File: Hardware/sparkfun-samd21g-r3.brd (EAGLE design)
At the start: 57.1 x 53.3 mm, 62 parts, among them Q1 2.5A/30V, Q2 2N7002PW, U1 MCP73831, U2 74AHC1G125, U3 MIC5219 3.3V, U4 ATSAMD21G-A, Y1 32.768kHz

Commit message: Swapping MIC5205 Regulator out for AP2112K-3.3V
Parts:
- U3: value MIC5219 3.3V -> 3.3V
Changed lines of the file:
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@@
 <layer number="47" name="Measures" color="7" fill="1" visible="no" active="yes"/>
 <layer number="48" name="Document" color="7" fill="1" visible="no" active="yes"/>
-<layer number="49" name="Reference" color="7" fill="1" visible="yes" active="yes"/>
+<layer number="49" name="Reference" color="7" fill="1" visible="no" active="yes"/>
 <layer number="50" name="dxf" color="7" fill="1" visible="no" active="no"/>
 <layer number="51" name="tDocu" color="6" fill="1" visible="yes" active="yes"/>
@@
 <attribute name="PROD_ID" value="IC-13064" x="38.1" y="30.48" size="1.778" layer="27" rot="R180" display="off"/>
 </element>
-<element name="U3" library="SparkFun-PowerIC" package="SOT23-5" value="MIC5219 3.3V" x="17.78" y="10.16" rot="R270">
-<attribute name="PROD_ID" value="VREG-09872" x="17.78" y="10.16" size="1.778" layer="27" rot="R270" display="off"/>
+<element name="U3" library="SparkFun-PowerIC" package="SOT23-5" value="3.3V" x="17.78" y="10.16" rot="R270">
+<attribute name="PROD_ID" value="VREG-12457" x="17.78" y="10.16" size="1.778" layer="27" rot="R270" display="off"/>
 </element>
 <element name="JP2" library="SparkFun-Connectors" package="USB-AB-MICRO-SMD_V03" value="" x="2.286" y="40.64">

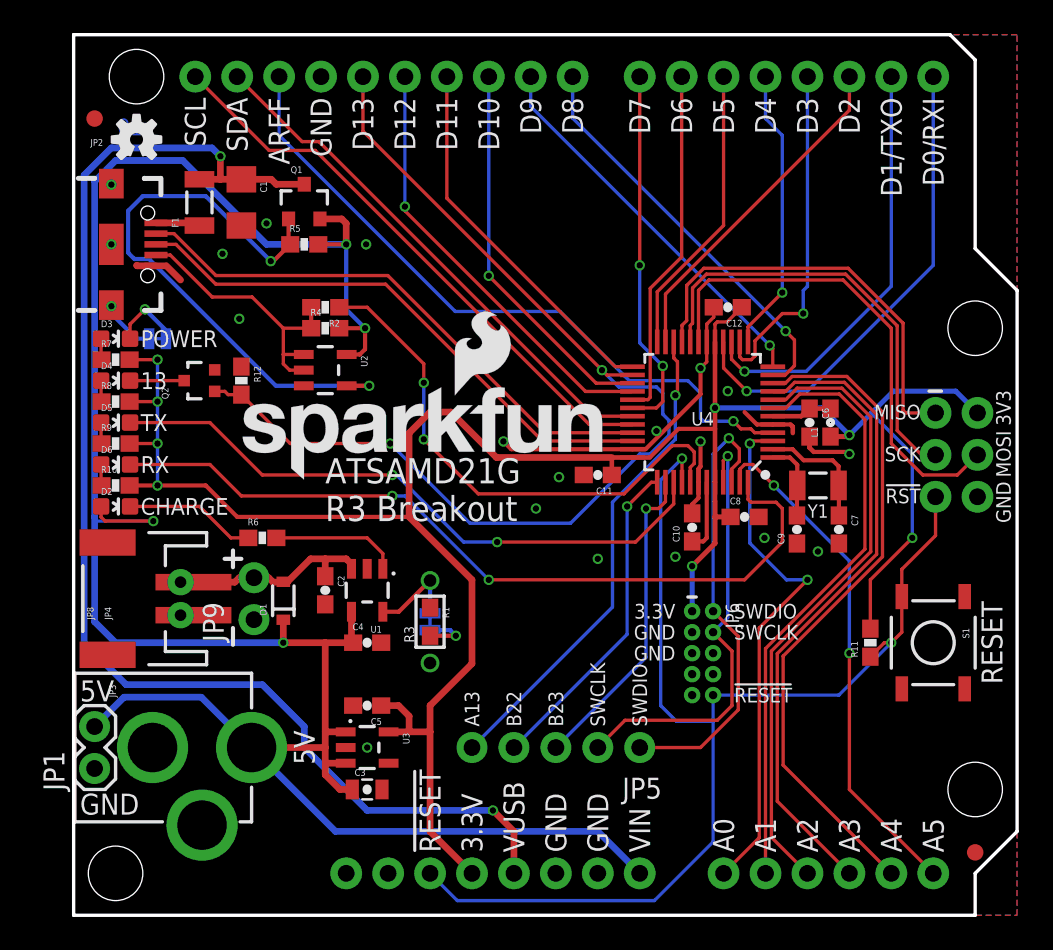
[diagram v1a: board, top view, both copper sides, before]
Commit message: Adding pin numbers to middle-board pins. Adding PWM indicators.
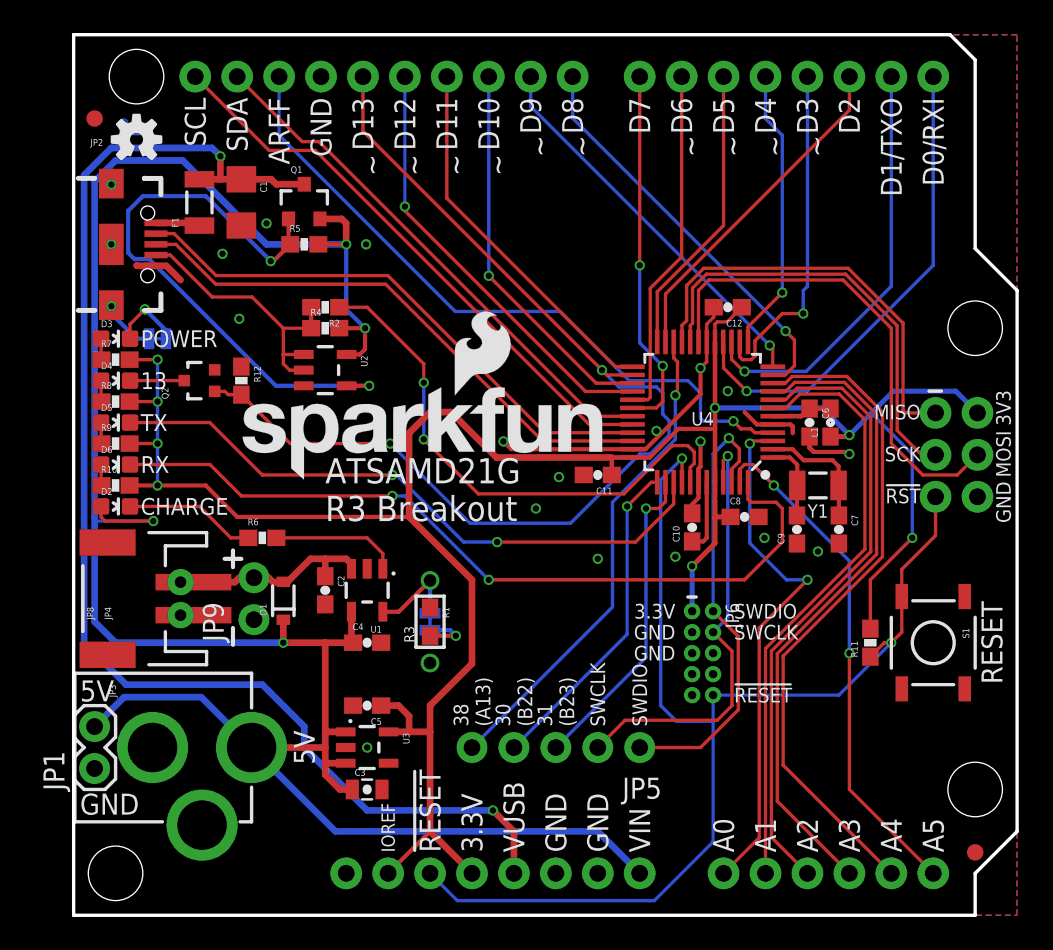
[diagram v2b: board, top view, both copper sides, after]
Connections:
- net 3.3V: now also JP7.IOREF
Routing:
- net 3.3V: track 143.7 -> 147.2 mm
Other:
- board text added: "30 (B22)"
- board text added: "31 (B23)"
- board text added: "38 (A13)"
- board text added: "IOREF"
- board text added: "~"
- board text removed: "A13"
- board text removed: "B22"
- board text removed: "B23"
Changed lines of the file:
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@@
 <layer number="47" name="Measures" color="7" fill="1" visible="no" active="yes"/>
 <layer number="48" name="Document" color="7" fill="1" visible="no" active="yes"/>
-<layer number="49" name="Reference" color="7" fill="1" visible="no" active="yes"/>
+<layer number="49" name="Reference" color="7" fill="1" visible="yes" active="yes"/>
 <layer number="50" name="dxf" color="7" fill="1" visible="no" active="no"/>
 <layer number="51" name="tDocu" color="6" fill="1" visible="yes" active="yes"/>
@@
 <text x="40.005" y="18.415" size="0.889" layer="21" font="vector" ratio="15" align="center-left">SWDIO</text>
 <text x="40.005" y="17.145" size="0.889" layer="21" font="vector" ratio="15" align="center-left">SWCLK</text>
-<text x="24.13" y="11.43" size="0.889" layer="21" font="vector" ratio="15" rot="R90" align="center-left">A13</text>
-<text x="26.67" y="11.43" size="0.889" layer="21" font="vector" ratio="15" rot="R90" align="center-left">B22</text>
-<text x="29.21" y="11.43" size="0.889" layer="21" font="vector" ratio="15" rot="R90" align="center-left">B23</text>
+<text x="24.13" y="11.43" size="0.889" layer="21" font="vector" ratio="15" rot="R90" align="center-left">38
+(A13)</text>
+<text x="26.67" y="11.43" size="0.889" layer="21" font="vector" ratio="15" rot="R90" align="center-left">30
+(B22)</text>
+<text x="29.21" y="11.43" size="0.889" layer="21" font="vector" ratio="15" rot="R90" align="center-left">31
+(B23)</text>
 <text x="20.32" y="17.78" size="0.889" layer="22" font="vector" ratio="15" rot="MR270" align="bottom-center">R-Prog</text>
 <text x="21.59" y="3.81" size="1.27" layer="22" font="vector" ratio="15" rot="MR270" align="center-right">!RESET!</text>
@@
 <wire x1="10.922" y1="16.637" x2="10.922" y2="15.621" width="0.254" layer="22"/>
 <wire x1="51.816" y1="31.75" x2="52.578" y2="31.75" width="0.2032" layer="21"/>
-<text x="24.13" y="11.43" size="0.889" layer="22" font="vector" ratio="15" rot="MR90" align="center-left">A13</text>
-<text x="26.67" y="11.43" size="0.889" layer="22" font="vector" ratio="15" rot="MR90" align="center-left">B22</text>
-<text x="29.21" y="11.43" size="0.889" layer="22" font="vector" ratio="15" rot="MR90" align="center-left">B23</text>
 <text x="31.75" y="11.43" size="0.889" layer="22" font="vector" ratio="15" rot="MR90" align="center-left">SWCLK</text>
 <text x="34.29" y="11.43" size="0.889" layer="22" font="vector" ratio="15" rot="MR90" align="center-left">SWDIO</text>
+<text x="24.13" y="11.43" size="0.889" layer="22" font="vector" ratio="15" rot="MR90" align="center-left">38
+(A13)</text>
+<text x="26.67" y="11.43" size="0.889" layer="22" font="vector" ratio="15" rot="MR90" align="center-left">30
+(B22)</text>
+<text x="29.21" y="11.43" size="0.889" layer="22" font="vector" ratio="15" rot="MR90" align="center-left">31
+(B23)</text>
+<text x="19.05" y="3.81" size="0.8128" layer="21" font="vector" ratio="15" rot="R90" align="center-left">IOREF</text>
+<text x="19.05" y="3.81" size="1.27" layer="22" font="vector" ratio="15" rot="MR90" align="center-left">IOREF</text>
+<text x="44.958" y="47.244" size="1.27" layer="21" font="vector" ratio="15" rot="R90" align="center-right">~</text>
+<text x="42.418" y="47.244" size="1.27" layer="21" font="vector" ratio="15" rot="R90" align="center-right">~</text>
+<text x="39.878" y="47.244" size="1.27" layer="21" font="vector" ratio="15" rot="R90" align="center-right">~</text>
+<text x="37.338" y="47.244" size="1.27" layer="21" font="vector" ratio="15" rot="R90" align="center-right">~</text>
+<text x="30.734" y="47.244" size="1.27" layer="21" font="vector" ratio="15" rot="R90" align="center-right">~</text>
+<text x="28.194" y="47.244" size="1.27" layer="21" font="vector" ratio="15" rot="R90" align="center-right">~</text>
+<text x="25.654" y="46.101" size="1.27" layer="21" font="vector" ratio="15" rot="R90" align="center-right">~</text>
+<text x="23.114" y="46.101" size="1.27" layer="21" font="vector" ratio="15" rot="R90" align="center-right">~</text>
+<text x="20.574" y="46.101" size="1.27" layer="21" font="vector" ratio="15" rot="R90" align="center-right">~</text>
+<text x="18.034" y="46.101" size="1.27" layer="21" font="vector" ratio="15" rot="R90" align="center-right">~</text>
+<text x="17.018" y="46.101" size="1.27" layer="22" font="vector" ratio="15" rot="MR90" align="center-right">~</text>
+<text x="19.558" y="46.101" size="1.27" layer="22" font="vector" ratio="15" rot="MR90" align="center-right">~</text>
+<text x="22.098" y="46.101" size="1.27" layer="22" font="vector" ratio="15" rot="MR90" align="center-right">~</text>
+<text x="24.638" y="46.101" size="1.27" layer="22" font="vector" ratio="15" rot="MR90" align="center-right">~</text>
+<text x="27.178" y="47.244" size="1.27" layer="22" font="vector" ratio="15" rot="MR90" align="center-right">~</text>
+<text x="29.718" y="47.244" size="1.27" layer="22" font="vector" ratio="15" rot="MR90" align="center-right">~</text>
+<text x="36.322" y="47.244" size="1.27" layer="22" font="vector" ratio="15" rot="MR90" align="center-right">~</text>
+<text x="38.862" y="47.244" size="1.27" layer="22" font="vector" ratio="15" rot="MR90" align="center-right">~</text>
+<text x="41.402" y="47.244" size="1.27" layer="22" font="vector" ratio="15" rot="MR90" align="center-right">~</text>
+<text x="43.942" y="47.244" size="1.27" layer="22" font="vector" ratio="15" rot="MR90" align="center-right">~</text>
 </plain>
 <attributes>
@@
 <wire x1="8.001" y1="26.035" x2="5.08" y2="26.035" width="0.254" layer="1"/>
 <wire x1="3.39" y1="26.035" x2="5.08" y2="26.035" width="0.254" layer="1"/>
+<contactref element="JP7" pad="IOREF"/>
+<wire x1="19.05" y1="2.54" x2="21.59" y2="5.08" width="0.254" layer="1"/>
 </signal>
 <signal name="VDDCORE">

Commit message: Tweaking schematic and layout silk for checklist
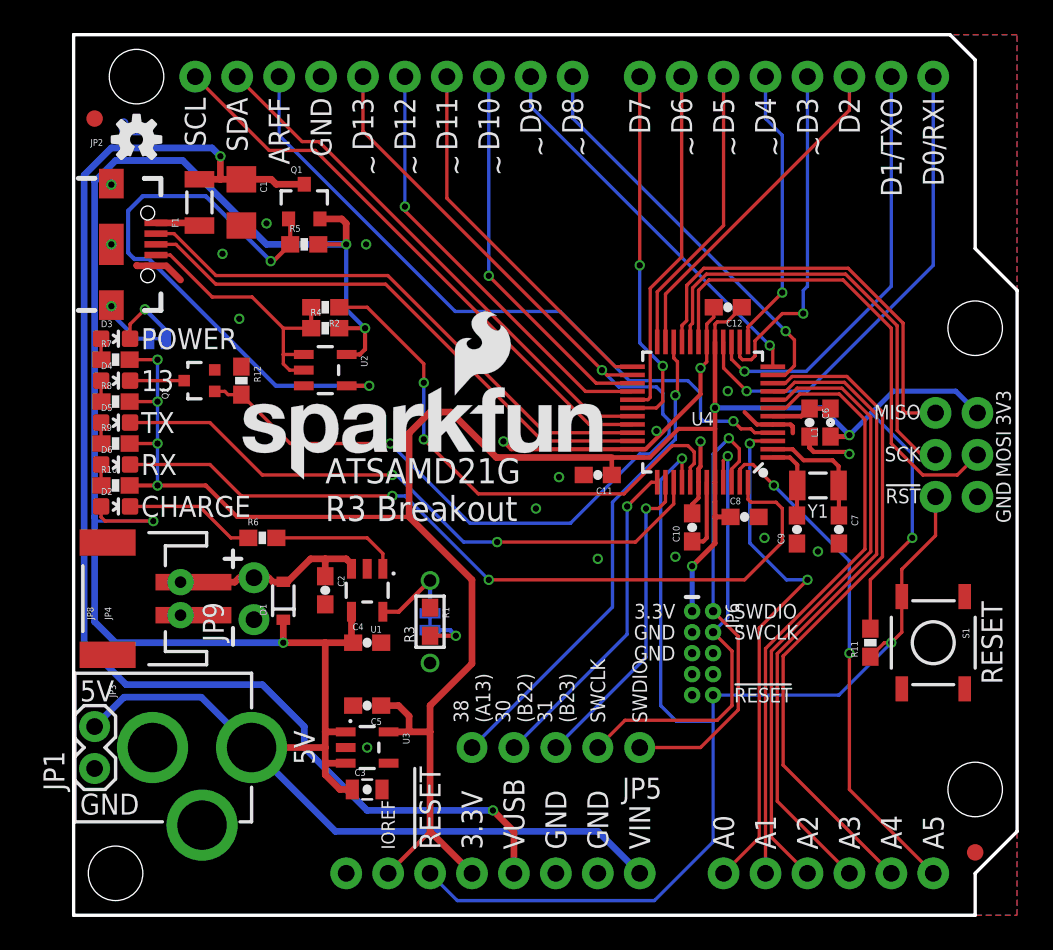
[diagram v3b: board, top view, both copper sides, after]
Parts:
- moved FRAME1 20.3 mm to (3.81, -29.2)
- moved LOGO4 2.29 mm to (14.6, 26.0)
- moved LOGO2 0.63 mm to (50.8, 6.99)
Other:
- board text added: "Units in inches"
